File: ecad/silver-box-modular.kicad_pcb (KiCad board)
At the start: 2 copper layers, 205 x 105 mm, 226 parts, among them J1 B6B-XH-A(LF)(SN), J10 B6B-XH-A(LF)(SN), J2 Amphenol_10061913-xx0, J3 Amphenol_10061913-xx0, J4 Amphenol_10061913-xx0, J5 Amphenol_10061913-xx0, J6 Amphenol_10061913-xx0, J7 Amphenol_10061913-xx0, J8 Amphenol_10061913-xx0, J9 Amphenol_10061913-xx0, SW1 KSC_SLT_241G_LFS, U1 CD4051BPWR4, U10 TLP4026G, U11 TLP4026G, U12 NE5532, U13 TLP4026G, U14 TLP4026G, U15 NE5532, U16 TLP4026G, U17 TLP4026G, U18 TCA9544APWR, U19 CD4051BPWR4, U2 NodeMCU ESP-32S, U20 CD4051BPWR4, U21 NE5532, U22 TLP4026G, U23 TLP4026G, U24 NE5532, U25 TLP4026G, U26 TLP4026G, U27 NE5532, U28 TLP4026G, U29 TLP4026G, U3 TCA9544APWR, U30 NE5532, U31 TLP4026G, U32 TLP4026G, U33 NE5532, U34 PGA231x, U4 CD4051BPWR4, U5 CD4051BPWR4, U6 NE5532, U7 TLP4026G, U8 TLP4026G, U9 NE5532

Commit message: Layout signal conditioning portion with approximate traces, update status and next steps in readme.
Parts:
- moved C49 102.8 mm to (237.7, -59.7)
- moved C50 102.8 mm to (248.1, -60.0)
- moved C51 102.8 mm to (257.8, -60.0)
- moved C52 102.8 mm to (268.1, -60.0)
- moved C53 102.8 mm to (278.1, -60.0)
- moved C54 102.8 mm to (288.1, -59.8)
- moved C55 102.8 mm to (298.1, -59.8)
- moved C56 102.8 mm to (307.9, -59.8)
- moved C57 102.8 mm to (318.1, -59.8)
- moved C58 102.8 mm to (328.1, -59.9)
- moved D1 102.8 mm to (237.5, -57.5)
- moved D10 102.8 mm to (327.5, -57.5)
- moved D2 102.8 mm to (247.5, -57.5)
- moved D3 102.8 mm to (257.5, -57.5)
- moved D4 102.8 mm to (267.5, -57.5)
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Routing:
- net GND: track 0.00 -> 15.9 mm
- net Net-(C6-Pad1): track 15.2 -> 5.57 mm
- net Net-(U6-Pad1): track 13.5 -> 22.5 mm
- net /~{Mute_CH1}: track 0.00 -> 7.50 mm
- net Net-(U6A--): track 4.97 -> 12.4 mm
- net Net-(U6B--): track 20.3 -> 13.5 mm
- net Net-(C7-Pad1): track 0.00 -> 6.63 mm
- net Net-(R14-Pad1): track 20.5 -> 14.8 mm
- net /BP_4Board_Control_and_Connect1/R_POMI_1: track 0.00 -> 5.60 mm
- net /BP_4Board_Control_and_Connect1/L_POMI_1: track 0.00 -> 5.60 mm
- net Net-(R12-Pad1): track 9.76 -> 4.16 mm
- net Net-(R13-Pad1): track 9.76 -> 4.16 mm
- net Net-(U6-Pad7): track 18.3 -> 23.8 mm
- net -12V: track 0.00 -> 2.86 mm
- net +12V: track 0.00 -> 2.86 mm
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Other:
- board text added: "- AOPI and MOPI will run on bottom layer - POMI needs review for critical paths but this might be close. - this could be denser but a little space is probably good for prototype. ToDo: - Trace width adjustments - Signal Ground planning"

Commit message: Continue board layout, partial power and digital signals are laid.
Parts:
- moved C14 60.1 mm to (83.5, 95.0)
- moved C15 60.0 mm to (101.5, 95.0)
- moved C38 59.9 mm to (226.5, 95.0)
- moved C37 59.8 mm to (208.5, 95.0)
- moved C25 59.8 mm to (133.5, 95.0)
- moved C30 59.6 mm to (176.5, 95.0)
- moved C29 59.5 mm to (158.5, 95.0)
- moved C34 59.5 mm to (201.5, 95.0)
- moved C26 59.5 mm to (151.5, 95.0)
- moved C18 59.4 mm to (108.5, 95.0)
- moved C19 59.4 mm to (126.5, 95.0)
- moved C33 59.3 mm to (183.5, 95.0)
- moved U13 49.5 mm to (87.5, 115.0), turned to 0 degrees
- moved U14 49.5 mm to (97.5, 115.0), turned to 0 degrees
- moved U31 49.3 mm to (212.5, 115.0), turned to 0 degrees
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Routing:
- net GND: track 15.9 -> 181.2 mm, vias 0 -> 27
- net -12V: track 2.86 -> 91.9 mm, vias 0 -> 5
- net +12V: track 2.86 -> 76.1 mm, vias 0 -> 5
- net /BP_4Board_Control_and_Connect1/Channel4/I2C_SDA: track 0.00 -> 64.1 mm
- net /BP_4Board_Control_and_Connect1/Channel4/I2C_SCL: track 0.00 -> 61.6 mm
- net /BP_4Board_Control_and_Connect1/Channel1/I2C_INT: track 0.00 -> 58.4 mm, vias 0 -> 2
- net /BP_4Board_Control_and_Connect1/Channel4/I2C_INT: track 0.00 -> 58.0 mm
- net /R_MOPI: track 0.00 -> 57.6 mm, vias 0 -> 3
- net /BP_4Board_Control_and_Connect1/Channel1/I2C_SCL: track 0.00 -> 50.5 mm
- net /BP_4Board_Control_and_Connect1/Channel1/I2C_SDA: track 0.00 -> 50.1 mm
- net /BP_4Board_Control_and_Connect1/R_POMI_1: track 5.60 -> 39.6 mm, vias 0 -> 2
- net /L_MOPI: track 0.00 -> 33.0 mm, vias 0 -> 2
- net /BP_4Board_Control_and_Connect1/Channel3/I2C_SDA: track 0.00 -> 29.7 mm
- net /BP_4Board_Control_and_Connect1/L_POMI_1: track 5.60 -> 31.4 mm, vias 0 -> 2
- net Net-(U10-Pad6): track 0.00 -> 23.4 mm
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- added copper zone on B.Cu, net GND
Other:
- board text added: "2023.03.15 Need to Consider teh analog power routing (+/-12) Probably will come from bottom layer and emerge in center under opamp. This should keep left right return paths undivided while allowing easy routing."
- board text removed: "- AOPI and MOPI will run on bottom layer - POMI needs review for critical paths but this might be close. - this could be denser but a little space is probably good for prototype. ToDo: - Trace width adjustments - Signal Ground planning"

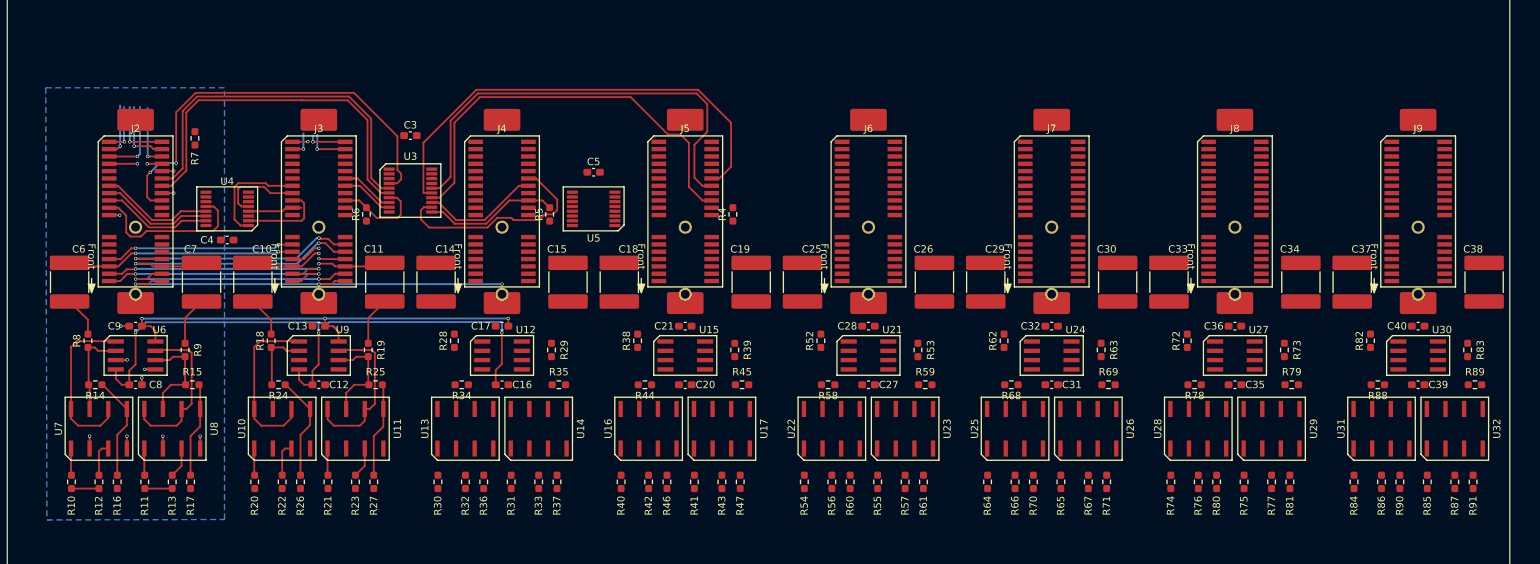
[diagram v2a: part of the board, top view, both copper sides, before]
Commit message: 2023.03.17 I2C out to master is current sticking point. Also needs review of grounds.
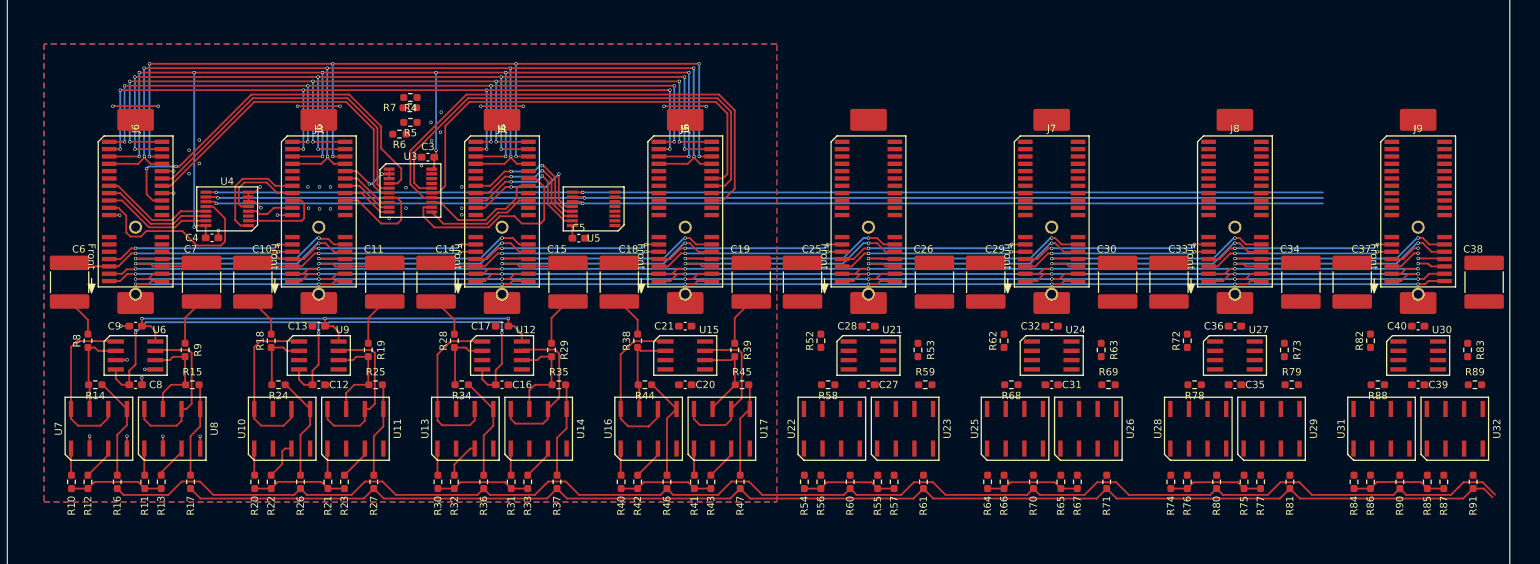
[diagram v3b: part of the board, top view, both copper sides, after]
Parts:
- moved R4 46.8 mm to (80.0, 69.8), turned to 180 degrees
- moved R7 29.6 mm to (79.9, 71.2), turned to 180 degrees
- moved R5 22.8 mm to (80.0, 73.2), turned to 180 degrees
- moved R6 11.8 mm to (78.5, 74.8), turned to 180 degrees
- moved C5 9.23 mm to (103.0, 89.0)
- moved C3 3.80 mm to (82.4, 78.0)
- moved C4 2.08 mm to (52.9, 89.0)
- moved R12 1.50 mm to (36.0, 122.2)
- moved R13 1.50 mm to (46.0, 122.2)
- moved R22 1.50 mm to (61.0, 122.2)
- moved R23 1.50 mm to (71.0, 122.2)
- moved R32 1.50 mm to (86.0, 122.2)
- moved R33 1.50 mm to (96.0, 122.2)
- moved R42 1.50 mm to (111.0, 122.2)
- moved R43 1.50 mm to (121.0, 122.2)
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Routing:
- net GND: track 181.2 -> 1303.8 mm, vias 27 -> 116
- net /BP_4Board_Control_and_Connect1/L_MSum: track 0.36 -> 205.5 mm
- net /BP_4Board_Control_and_Connect1/R_MSum: track 0.00 -> 186.0 mm
- net /L_MOPI: track 33.0 -> 207.0 mm, vias 2 -> 8
- net +3V3: track 10.7 -> 176.8 mm, vias 1 -> 12
- net /ID_ADDR_1: track 0.00 -> 154.2 mm, vias 0 -> 2
- net /ID_ADDR_0: track 0.00 -> 154.0 mm, vias 0 -> 2
- net /ID_ADDR_2: track 0.00 -> 153.8 mm, vias 0 -> 2
- net /R_MOPI: track 57.6 -> 206.2 mm, vias 3 -> 8
- net +5V: track 8.55 -> 132.4 mm, vias 1 -> 8
- net +12V: track 76.1 -> 190.1 mm, vias 5 -> 11
- net -12V: track 91.9 -> 200.4 mm, vias 5 -> 11
- net /BP_4Board_Control_and_Connect1/R_POMI_3: track 0.00 -> 39.6 mm, vias 0 -> 2
- net /BP_4Board_Control_and_Connect2/R_POMI_3: track 0.00 -> 34.0 mm, vias 0 -> 2
- net /BP_4Board_Control_and_Connect2/R_POMI_1: track 0.00 -> 34.0 mm, vias 0 -> 2
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- added copper zone on F.Cu, net GND
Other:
- board text added: "2023.03.17 I2C out to master is current sticvking point. Needs review of grounds."
- board text added: "J6"
- board text removed: "2023.03.15 Need to Consider teh analog power routing (+/-12) Probably will come from bottom layer and emerge in center under opamp. This should keep left right return paths undivided while allowing easy routing."

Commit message: Route mutes and i2c master, rough positioning of esp32, will likely move towards a corner later.
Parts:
- moved J1 161.2 mm to (109.1, 48.7), turned to -90 degrees
- moved U1 139.1 mm to (178.7, 56.9), turned to 90 degrees
- moved C1 137.2 mm to (176.7, 61.0), turned to 0 degrees
- moved TP8 134.4 mm to (172.5, 42.5)
- moved C2 131.0 mm to (164.9, 63.8)
- moved U2 130.6 mm to (143.5, 49.0)
- moved R1 128.7 mm to (128.4, 33.7), turned to -90 degrees
- moved TP7 128.1 mm to (177.5, 42.5)
- moved R3 126.2 mm to (130.9, 33.7), turned to -90 degrees
- moved TP2 124.9 mm to (185.0, 47.5)
- moved R2 124.2 mm to (138.4, 33.7), turned to -90 degrees
- moved TP4 120.9 mm to (175.0, 47.5)
- moved TP6 120.2 mm to (182.5, 42.5)
- moved TP1 119.4 mm to (190.0, 47.5)
- moved TP3 114.6 mm to (180.0, 47.5)
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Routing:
- net /~{Mute_CH1}: track 13.0 -> 256.9 mm
- net /~{Mute_CH2}: track 13.0 -> 241.1 mm
- net /~{Mute_CH3}: track 13.0 -> 213.5 mm
- net /~{Mute_CH4}: track 13.0 -> 187.6 mm
- net /~{Mute_CH5}: track 13.0 -> 162.1 mm
- net /~{Mute_CH6}: track 13.0 -> 136.0 mm
- net /~{Mute_CH7}: track 13.0 -> 110.0 mm
- net /I2C_SDA: track 0.00 -> 77.4 mm, vias 0 -> 1
- net /I2C_SCL: track 0.00 -> 74.5 mm, vias 0 -> 1
- net /~{I2C_INT}: track 0.00 -> 73.5 mm, vias 0 -> 1
- net /~{Mute_CH8}: track 13.0 -> 84.2 mm
- net -12V: track 200.4 -> 244.5 mm, vias 11 -> 12
- net +12V: track 190.1 -> 227.7 mm, vias 11 -> 12
- net /BP_4Board_Control_and_Connect1/R_MSum: track 186.0 -> 155.1 mm, vias 0 -> 2
- net /BP_4Board_Control_and_Connect1/L_MSum: track 205.5 -> 177.6 mm, vias 0 -> 2
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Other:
- board text added: "2023.03.18 * Look for ways to shrink x to below 200mm * Look into multiboard project for control board * Needs review of grounds."
- board text removed: "2023.03.17 I2C out to master is current sticvking point. Needs review of grounds."

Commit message: Route all traces, needs review. Still needs silkscreen cleanup and conversion to true two board file.
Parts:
- J10: moved to B.Cu
- moved R93 171.0 mm to (44.0, 58.5), turned to 180 degrees
- moved C42 170.0 mm to (40.2, 53.5), turned to -90 degrees
- moved U33 166.1 mm to (43.8, 53.3), turned to 180 degrees
- moved C41 162.0 mm to (47.4, 53.0), turned to 90 degrees
- moved R92 159.5 mm to (45.4, 48.1), turned to 180 degrees
- moved C44 157.8 mm to (59.8, 61.3), turned to 0 degrees
- moved C48 157.3 mm to (50.9, 52.9), turned to 90 degrees
- moved U34 150.2 mm to (58.1, 52.8), turned to -90 degrees
- moved C46 143.2 mm to (65.9, 52.9), turned to 90 degrees
- moved C47 141.2 mm to (69.3, 53.8), turned to 180 degrees
- moved C43 140.0 mm to (59.6, 44.3), turned to 0 degrees
- moved C45 139.0 mm to (69.3, 52.0), turned to 180 degrees
- moved RV1 122.6 mm to (255.0, 90.0)
- moved C58 121.5 mm to (277.5, 50.5)
- moved R103 121.2 mm to (277.5, 48.8)
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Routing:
- net GND: track 1303.8 -> 2421.7 mm, vias 139 -> 345
- net -12V: track 244.5 -> 610.4 mm, vias 12 -> 27
- net +12V: track 227.7 -> 580.1 mm, vias 12 -> 28
- net +3V3: track 176.8 -> 475.2 mm, vias 12 -> 37
- net +5V: track 132.4 -> 341.3 mm, vias 8 -> 18
- net +5VL: track 0.00 -> 207.2 mm, vias 0 -> 22
- net /Vol_SDI: track 0.00 -> 167.0 mm, vias 0 -> 1
- net /Vol_SDO: track 0.00 -> 164.1 mm, vias 0 -> 3
- net /Vol_SCLK: track 0.00 -> 162.5 mm, vias 0 -> 1
- net /~{Mute_CH0}: track 0.00 -> 159.8 mm, vias 0 -> 3
- net /~{Vol_CS}: track 0.00 -> 157.2 mm, vias 0 -> 1
- net /Vol_ZeroX_EN: track 0.00 -> 146.6 mm, vias 0 -> 1
- net /BP_4Board_Control_and_Connect1/R_MSum: track 155.1 -> 292.9 mm, vias 2 -> 9
- net /L_MOPI: track 207.0 -> 330.9 mm, vias 8 -> 9
- net /R_MOPI: track 206.2 -> 326.7 mm, vias 8 -> 9
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- added copper zone on B.Cu, net GND1
- removed copper zone on F.Cu, net GND
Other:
- board size 205 x 105 mm -> 250 x 100 mm

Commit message: Full layout for review after checking mechanical assembly.
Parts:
- added REF**: MountingHole_3.2mm_M3, MountingHole:MountingHole_3.2mm_M3, F.Cu at (235.0, 55.5)
- added REF**: MountingHole_2.2mm_M2, MountingHole:MountingHole_2.2mm_M2, F.Cu at (47.5, 125.5)
- added REF**: MountingHole_2.2mm_M2, MountingHole:MountingHole_2.2mm_M2, F.Cu at (47.5, 95.5)
- added REF**: MountingHole_2.2mm_M2, MountingHole:MountingHole_2.2mm_M2, F.Cu at (217.5, 55.5)
- added REF**: MountingHole_2.2mm_M2, MountingHole:MountingHole_2.2mm_M2, F.Cu at (27.5, 55.5)
- added REF**1: MountingHole_3.2mm_M3, MountingHole:MountingHole_3.2mm_M3, F.Cu at (275.0, 55.5)
- added REF**10: MountingHole_2.2mm_M2, MountingHole:MountingHole_2.2mm_M2, F.Cu at (97.5, 95.5)
- added REF**11: MountingHole_2.2mm_M2, MountingHole:MountingHole_2.2mm_M2, F.Cu at (147.5, 95.5)
- added REF**12: MountingHole_2.2mm_M2, MountingHole:MountingHole_2.2mm_M2, F.Cu at (197.5, 95.5)
- added REF**2: MountingHole_3.2mm_M3, MountingHole:MountingHole_3.2mm_M3, F.Cu at (235.0, 145.5)
- added REF**3: MountingHole_3.2mm_M3, MountingHole:MountingHole_3.2mm_M3, F.Cu at (275.0, 145.5)
- added REF**4: MountingHole_2.2mm_M2, MountingHole:MountingHole_2.2mm_M2, F.Cu at (72.5, 125.5)
- added REF**5: MountingHole_2.2mm_M2, MountingHole:MountingHole_2.2mm_M2, F.Cu at (97.5, 125.5)
- added REF**6: MountingHole_2.2mm_M2, MountingHole:MountingHole_2.2mm_M2, F.Cu at (122.5, 125.5)
- added REF**7: MountingHole_2.2mm_M2, MountingHole:MountingHole_2.2mm_M2, F.Cu at (147.5, 125.5)
- added REF**8: MountingHole_2.2mm_M2, MountingHole:MountingHole_2.2mm_M2, F.Cu at (172.5, 125.5)
- added REF**9: MountingHole_2.2mm_M2, MountingHole:MountingHole_2.2mm_M2, F.Cu at (197.5, 125.5)
- added control_plate: Board, PCM_kikit:Board, F.Cu at (242.5, 50.5)
- added mainboard: Board, PCM_kikit:Board, F.Cu at (40.0, 50.5)
- moved C58 93.2 mm to (235.0, 133.5)
- moved D10 93.2 mm to (235.0, 135.5)
- moved R103 93.2 mm to (235.0, 131.8)
- moved C57 88.3 mm to (242.5, 133.5)
- moved D9 88.3 mm to (242.5, 135.5)
- moved R102 88.3 mm to (242.5, 131.8)
- moved C55 83.9 mm to (275.0, 133.5)
- moved D7 83.9 mm to (275.0, 135.5)
- moved R100 83.9 mm to (275.0, 131.8)
- moved C56 83.0 mm to (267.5, 133.5)
- moved D8 83.0 mm to (267.5, 135.5)
- moved R101 83.0 mm to (267.5, 131.8)
- moved TP5 26.6 mm to (212.5, 70.5)
- moved TP6 26.6 mm to (219.2, 70.5)
- moved TP7 26.3 mm to (212.5, 63.0)
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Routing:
- net Net-(D6-DOut): track 10.3 -> 61.1 mm
- net +5VL: track 207.2 -> 240.3 mm, vias 22 -> 23
- net Net-(D8-DOut): track 10.3 -> 32.2 mm
- net Net-(U2-IO04/I2S_BC): track 32.4 -> 37.9 mm
- net Net-(U2-IO18/I2S_DOUT): track 36.8 -> 42.0 mm
- net Net-(U2-IO05/I2S_WS): track 46.2 -> 51.3 mm
- net /BP_4Board_Control_and_Connect2/Channel4/I2C_INT: track 80.5 -> 84.8 mm
- net /BP_4Board_Control_and_Connect1/Channel1/I2C_SCL: track 45.0 -> 48.8 mm
- net /BP_4Board_Control_and_Connect1/Channel1/I2C_SDA: track 44.7 -> 48.5 mm
- net GND: track 2421.7 -> 2418.0 mm, vias 345 -> 340
- net /BP_4Board_Control_and_Connect2/Channel4/I2C_SCL: track 65.6 -> 69.2 mm
- net /BP_4Board_Control_and_Connect2/Channel4/I2C_SDA: track 61.9 -> 65.4 mm
- net /BP_4Board_Control_and_Connect1/Channel4/I2C_INT: track 76.4 -> 79.5 mm
- net /BP_4Board_Control_and_Connect1/Channel1/I2C_INT: track 54.4 -> 57.5 mm
- net /BP_4Board_Control_and_Connect1/Channel4/I2C_SDA: track 61.9 -> 64.7 mm
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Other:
- board size 250 x 100 mm -> 257.5 x 100 mm
- board text removed: "2023.03.18 * Look for ways to shrink x to below 200mm * Look into multiboard project for control board * Needs review of grounds."
